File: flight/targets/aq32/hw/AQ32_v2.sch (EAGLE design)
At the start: 118 parts, among them Q2 BCV27, Q3 BCV27, Q5 BCV27, Q6 BCV27, U1 ITG-3200, U10 MS5611, U11 MIC5239, U13 74AHC1G86DCK, U2 STM32F10XVXT6, U3 74AHC1G86DCK, U7 USD-SOCKETNEW, U9 HMC5883LSMD, X2 USBOLD

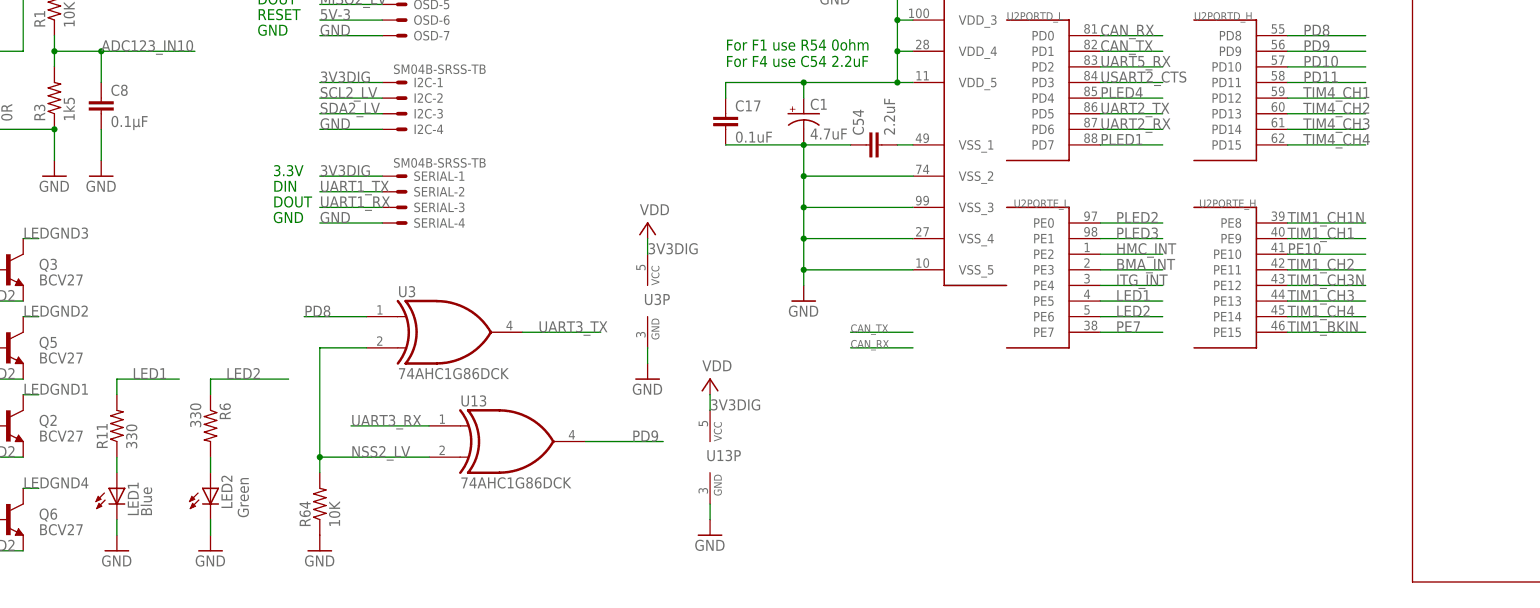
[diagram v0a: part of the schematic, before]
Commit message: 20150724 - Add license to schematic file, add pdf print of schematic.
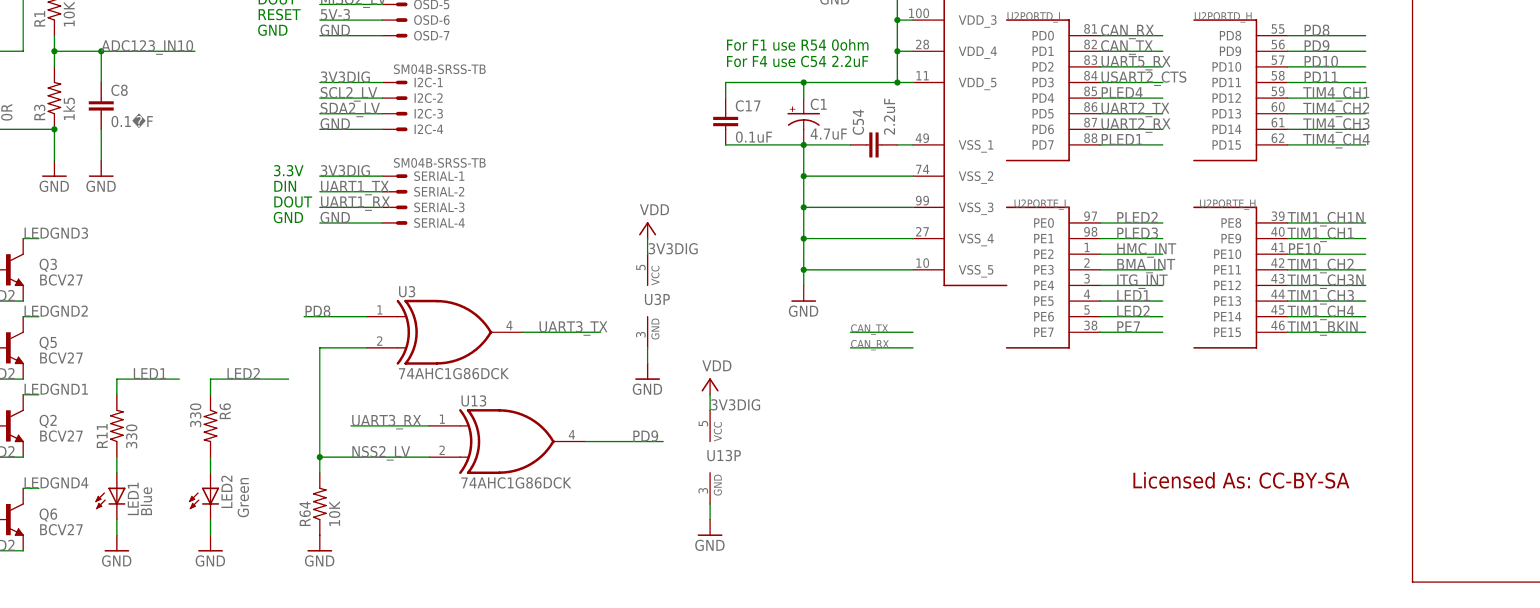
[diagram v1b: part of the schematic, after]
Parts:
- C8: value 0.1µF -> 0.1�F
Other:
- note added: "Licensed As: CC-BY-SA"
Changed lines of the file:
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@@
 <?xml version="1.0" encoding="utf-8"?>
 <!DOCTYPE eagle SYSTEM "eagle.dtd">
-<eagle version="6.4">
+<eagle version="7.3.0">
 <drawing>
 <settings>
@@
 <part name="SUPPLY1" library="supply2" deviceset="V+" device="" value="VDD"/>
 <part name="GND37" library="SparkFun" deviceset="GND" device=""/>
-<part name="C8" library="SparkFun" deviceset="CAP" device="0402" value="0.1µF"/>
+<part name="C8" library="SparkFun" deviceset="CAP" device="0402" value="0.1�F"/>
 <part name="GND39" library="SparkFun" deviceset="GND" device=""/>
 <part name="C15" library="SparkFun" deviceset="CAP" device="0402" value="0.1uF"/>
@@
 <text x="142.24" y="86.36" size="1.778" layer="91">For F1 use R54 0ohm
 For F4 use C54 2.2uF</text>
+<text x="208.28" y="17.78" size="2.54" layer="94">Licensed As: CC-BY-SA</text>
 </plain>
 <instances>
